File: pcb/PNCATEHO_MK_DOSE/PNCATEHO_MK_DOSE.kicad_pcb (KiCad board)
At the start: 2 copper layers, 97 x 59 mm, 47 parts, among them J1 TestPoint_2Pole, U1 ProMicro_r

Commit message: PNCATEHO MK-DOSE routed
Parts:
- removed LED1, LED10, LED2, LED3, LED4, LED5, LED6, LED7, LED8, LED9: YS-SK6812MINI-E, PNCATEHO:YS-SK6812MINI-E_duplex
- added D21: LED, PNCATEHO:0603-led_dual, F.Cu at (110.0, 61.2)
- added D22: LED, PNCATEHO:0603-led_dual, F.Cu at (113.0, 61.2)
- added D23: LED, PNCATEHO:0603-led_dual, F.Cu at (116.0, 61.2)
- added R1: R, PNCATEHO:0603-resistor_dual, F.Cu at (110.0, 62.7)
- added R2: R, PNCATEHO:0603-resistor_dual, F.Cu at (113.0, 62.7)
- added R3: R, PNCATEHO:0603-resistor_dual, F.Cu at (116.0, 62.7)
- D1, D10, D11, D12, D13, D14, D15, D16, D17, D18, D19, D2, D20, D3, D4, D5, D6, D7, D8, D9: footprint Diode_SMD:D_SOD-123 -> PNCATEHO:D3_SMD
- PSW1: value SW_SPDT -> ~; footprint PNCATEHO:MSK-12C02_DUAL -> PNCATEHO:bsi10h
- moved D20 109.5 mm to (113.0, 82.0)
- moved D18 102.1 mm to (94.0, 82.0)
- moved D19 101.1 mm to (113.0, 66.0)
- moved D16 92.4 mm to (94.0, 63.0)
- moved D17 92.2 mm to (94.0, 66.0)
- moved D8 84.2 mm to (94.0, 44.0)
- moved D7 78.2 mm to (94.0, 28.0)
- moved D15 77.3 mm to (94.0, 47.0)
- moved D14 76.3 mm to (75.0, 63.0)
- moved D6 73.4 mm to (75.0, 44.0)
- moved D12 72.6 mm to (56.0, 63.0)
- moved D13 66.7 mm to (75.0, 47.0)
- moved D5 62.1 mm to (75.0, 28.0)
- moved D11 61.1 mm to (56.0, 47.0)
- moved D10 58.9 mm to (37.0, 63.0)
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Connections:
- J1 pad 1: Net-(PSW1-B) -> Net-(J1-Pad1)
- PSW1 pad 1: VBAT -> Net-(J1-Pad1)
- PSW1 pad 2: Net-(PSW1-B) -> VBAT
- U1 pad 10: R0 -> C1
- U1 pad 11: R1 -> R3
- U1 pad 12: LED -> R5
- U1 pad 13: R5 -> R4
- U1 pad 14: R4 -> unconnected-(U1-16/B2-Pad14)_1
- U1 pad 15: R3 -> R2
- U1 pad 16: R2 -> C3
- U1 pad 17: C3 -> C2
- U1 pad 18: C2 -> R1
- U1 pad 19: C1 -> C0
- U1 pad 20: C0 -> R0
- U1 pad 21: VCC -> unconnected-(U1-VCC-Pad21)
- U1 pad 7: unconnected-(U1-D4/4-Pad7)_1 -> LED0
- U1 pad 8: unconnected-(U1-C6/5-Pad8)_1 -> LED1
- U1 pad 9: unconnected-(U1-D7/6-Pad9) -> LED2
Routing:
- net C2: track 0.00 -> 142.1 mm, vias 0 -> 7
- net C0: track 0.00 -> 140.9 mm, vias 0 -> 5
- net C1: track 0.00 -> 124.9 mm, vias 0 -> 6
- net C3: track 0.00 -> 122.4 mm, vias 0 -> 7
- net R2: track 0.00 -> 104.6 mm, vias 0 -> 5
- net R0: track 0.00 -> 104.6 mm, vias 0 -> 5
- net R1: track 0.00 -> 100.4 mm, vias 0 -> 5
- net R3: track 0.00 -> 97.1 mm, vias 0 -> 6
- net VBAT: track 0.00 -> 75.7 mm, vias 0 -> 1
- net R5: track 0.00 -> 68.7 mm, vias 0 -> 3
- net reset: track 0.00 -> 63.3 mm, vias 0 -> 1
- net Net-(J1-Pad1): track 0.00 -> 61.4 mm
- net R4: track 0.00 -> 54.5 mm, vias 0 -> 3
- net LED0: track 0.00 -> 28.5 mm, vias 0 -> 1
- net LED1: track 0.00 -> 24.9 mm, vias 0 -> 1
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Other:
- board size 97 x 59 mm -> 95 x 57 mm
- board text added: "A"
- board text added: "C"
- board text added: "E"
- board text added: "H"
- board text added: "N"
- board text added: "O"
- board text added: "P"
- board text added: "PNCATEHO MK-DOSE"
- board text added: "T"
- board text added: "by Aorum/turtle"
- board text removed: "PCB Designed by Aorum/turtle VMK-DOSE"
- board text removed: "PNCATEHO V0.5"
- board text removed: "А"
- board text removed: "Е"
- board text removed: "И"
- board text removed: "Н"
- board text removed: "О"
- board text removed: "Р"
- board text removed: "С"
- board text removed: "Т"

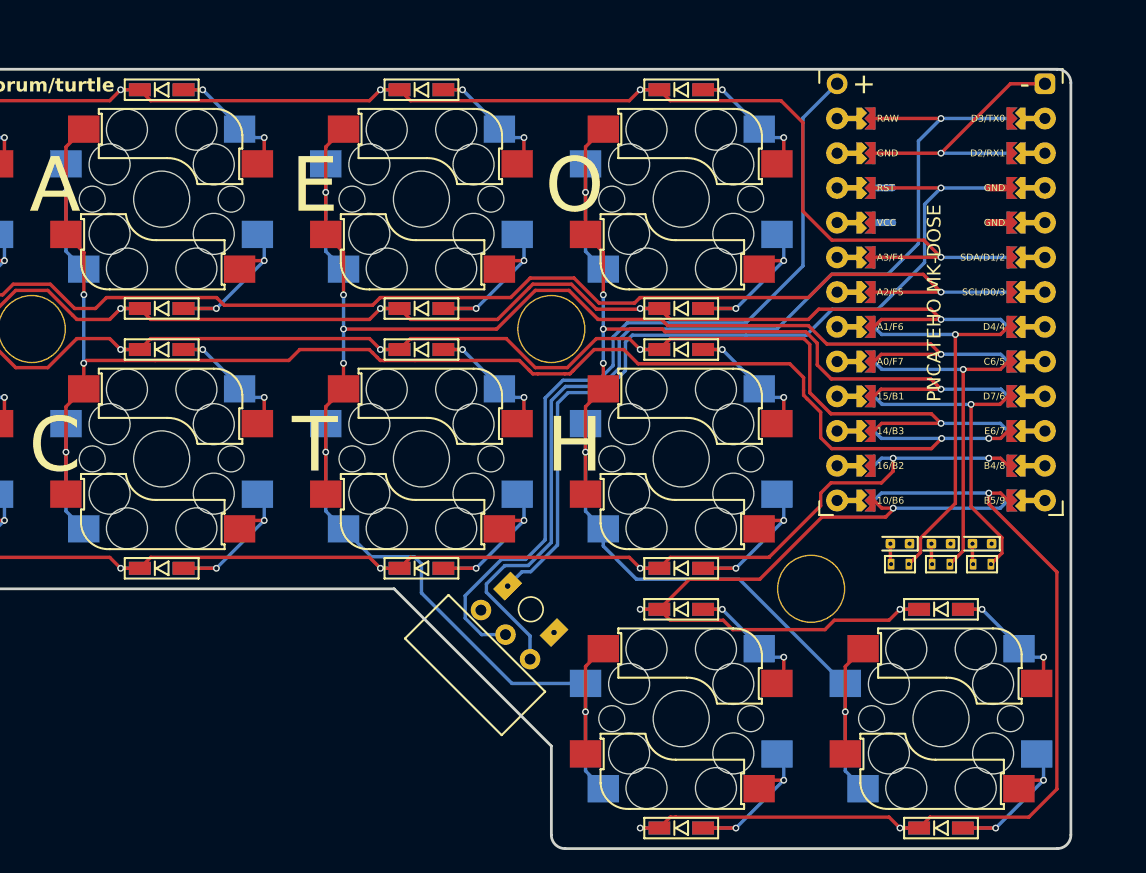
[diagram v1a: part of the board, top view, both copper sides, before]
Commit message: MK-DOSE version, with 100x100 version
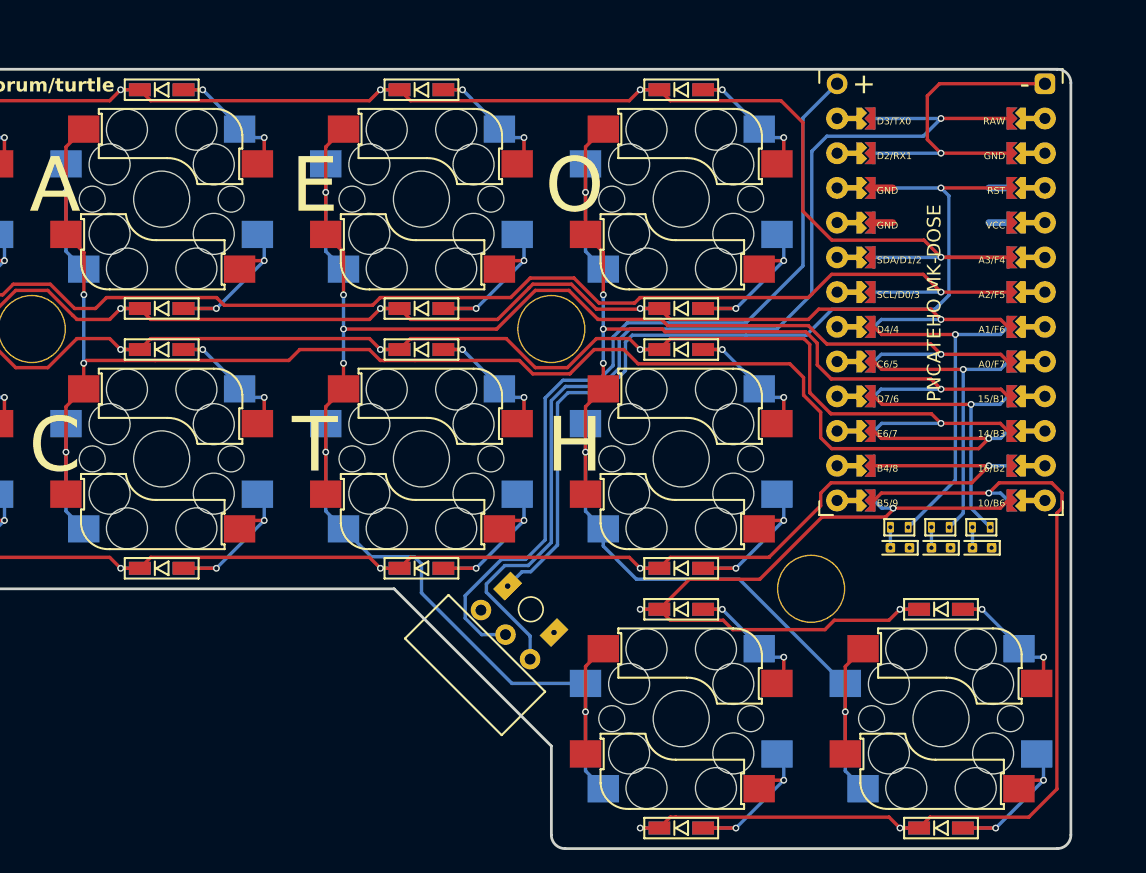
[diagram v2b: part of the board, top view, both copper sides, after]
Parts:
- U1: footprint PNCATEHO:ProMicro_duplex -> PNCATEHO:ProMicro_duplex_mirrored
- moved R1 2.70 mm to (110.0, 60.0)
- moved R2 2.70 mm to (113.0, 60.0)
- moved R3 2.70 mm to (116.0, 60.0)
- moved D21 0.30 mm to (110.0, 61.5)
- moved D22 0.30 mm to (113.0, 61.5)
- moved D23 0.30 mm to (116.0, 61.5)
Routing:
- net R3: track 97.1 -> 103.0 mm, vias 6 -> 5
- net R0: track 104.6 -> 109.5 mm
- net R5: track 68.7 -> 72.8 mm
- net Net-(J1-Pad2): track 19.5 -> 23.4 mm
- net C1: track 124.9 -> 128.3 mm, vias 6 -> 5
- net LED2: track 23.2 -> 19.9 mm
- net reset: track 63.3 -> 66.3 mm
- net LED1: track 24.9 -> 22.2 mm
- net LED0: track 28.5 -> 25.8 mm
- net VBAT: track 75.7 -> 77.4 mm
